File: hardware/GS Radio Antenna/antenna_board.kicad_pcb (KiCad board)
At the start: 2 copper layers, 100 x 100 mm, 22 parts, among them J1 Conn_01x02_Socket, U10 IRF4905PBF, U11 IRF4905PBF, U12 IRF4905PBF, U2 ESP32-DEVKITC, U3 LM3940IT-3.3/NOPB, U4 TLC5916IN, U5 TLC5916IN, U6 TLC5916IN, U9 IRF4905PBF

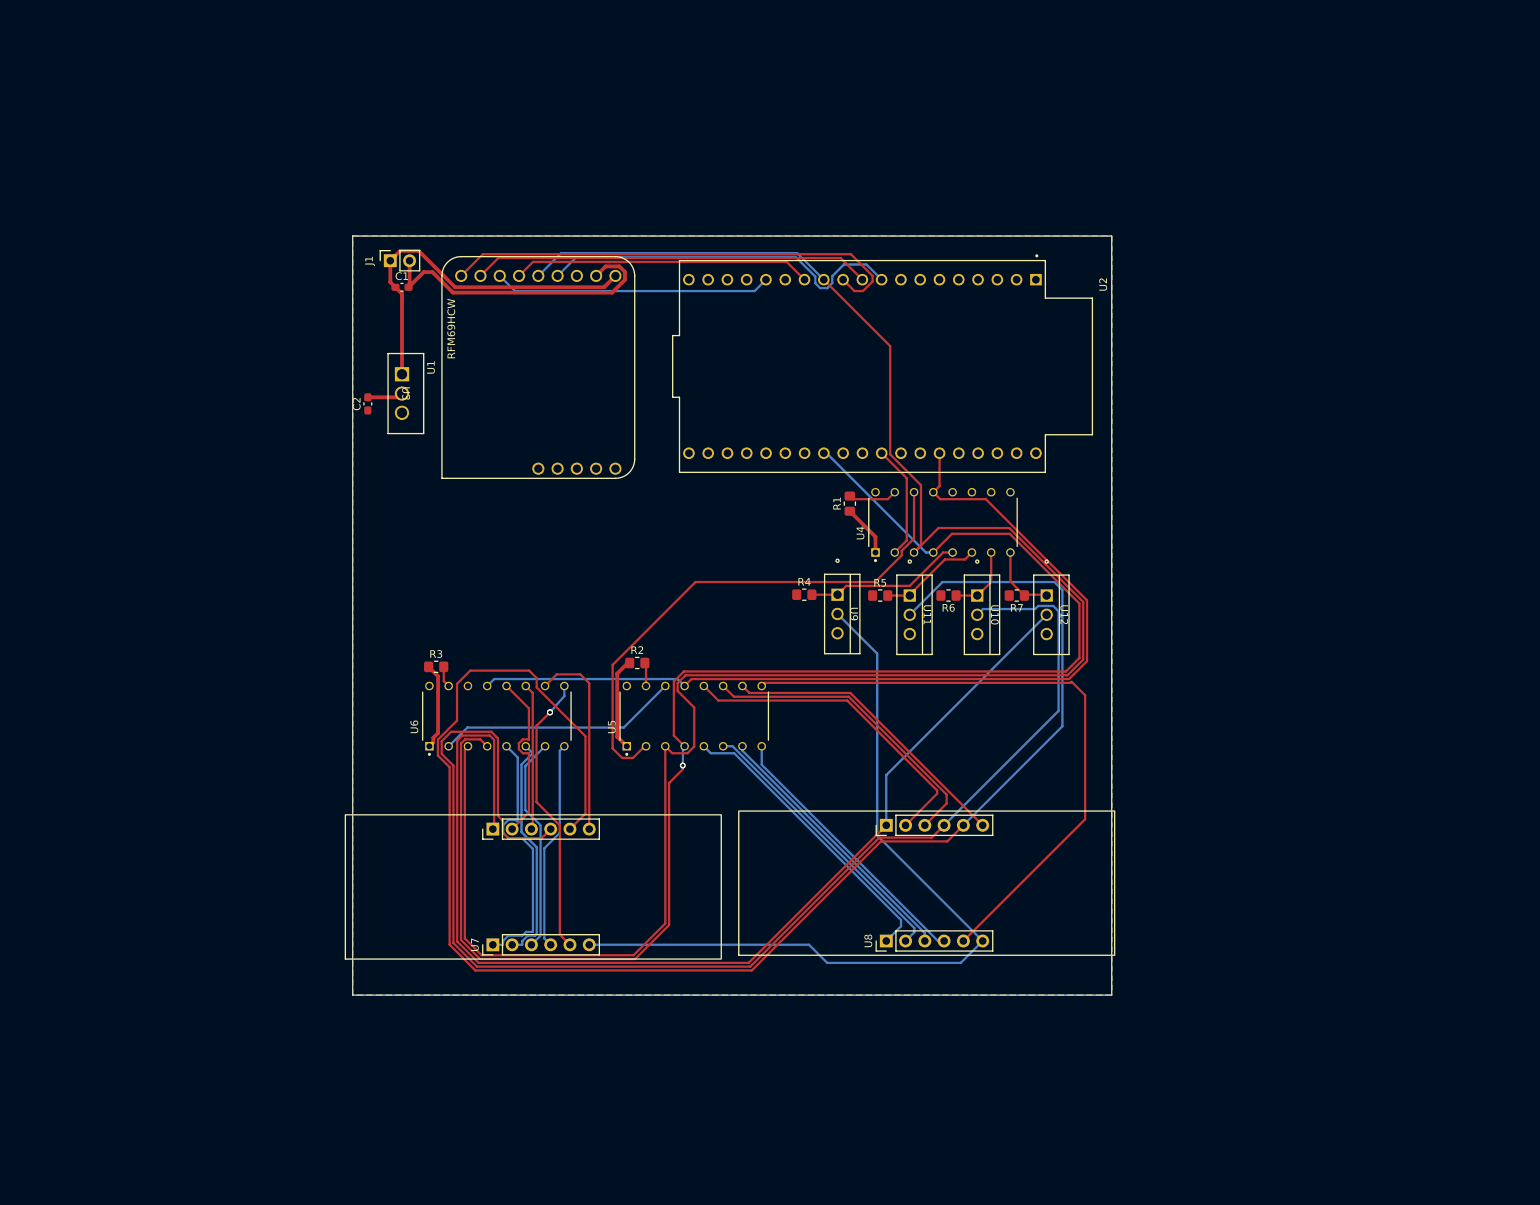
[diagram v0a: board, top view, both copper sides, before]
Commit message: New GS Radio board layout without wiring
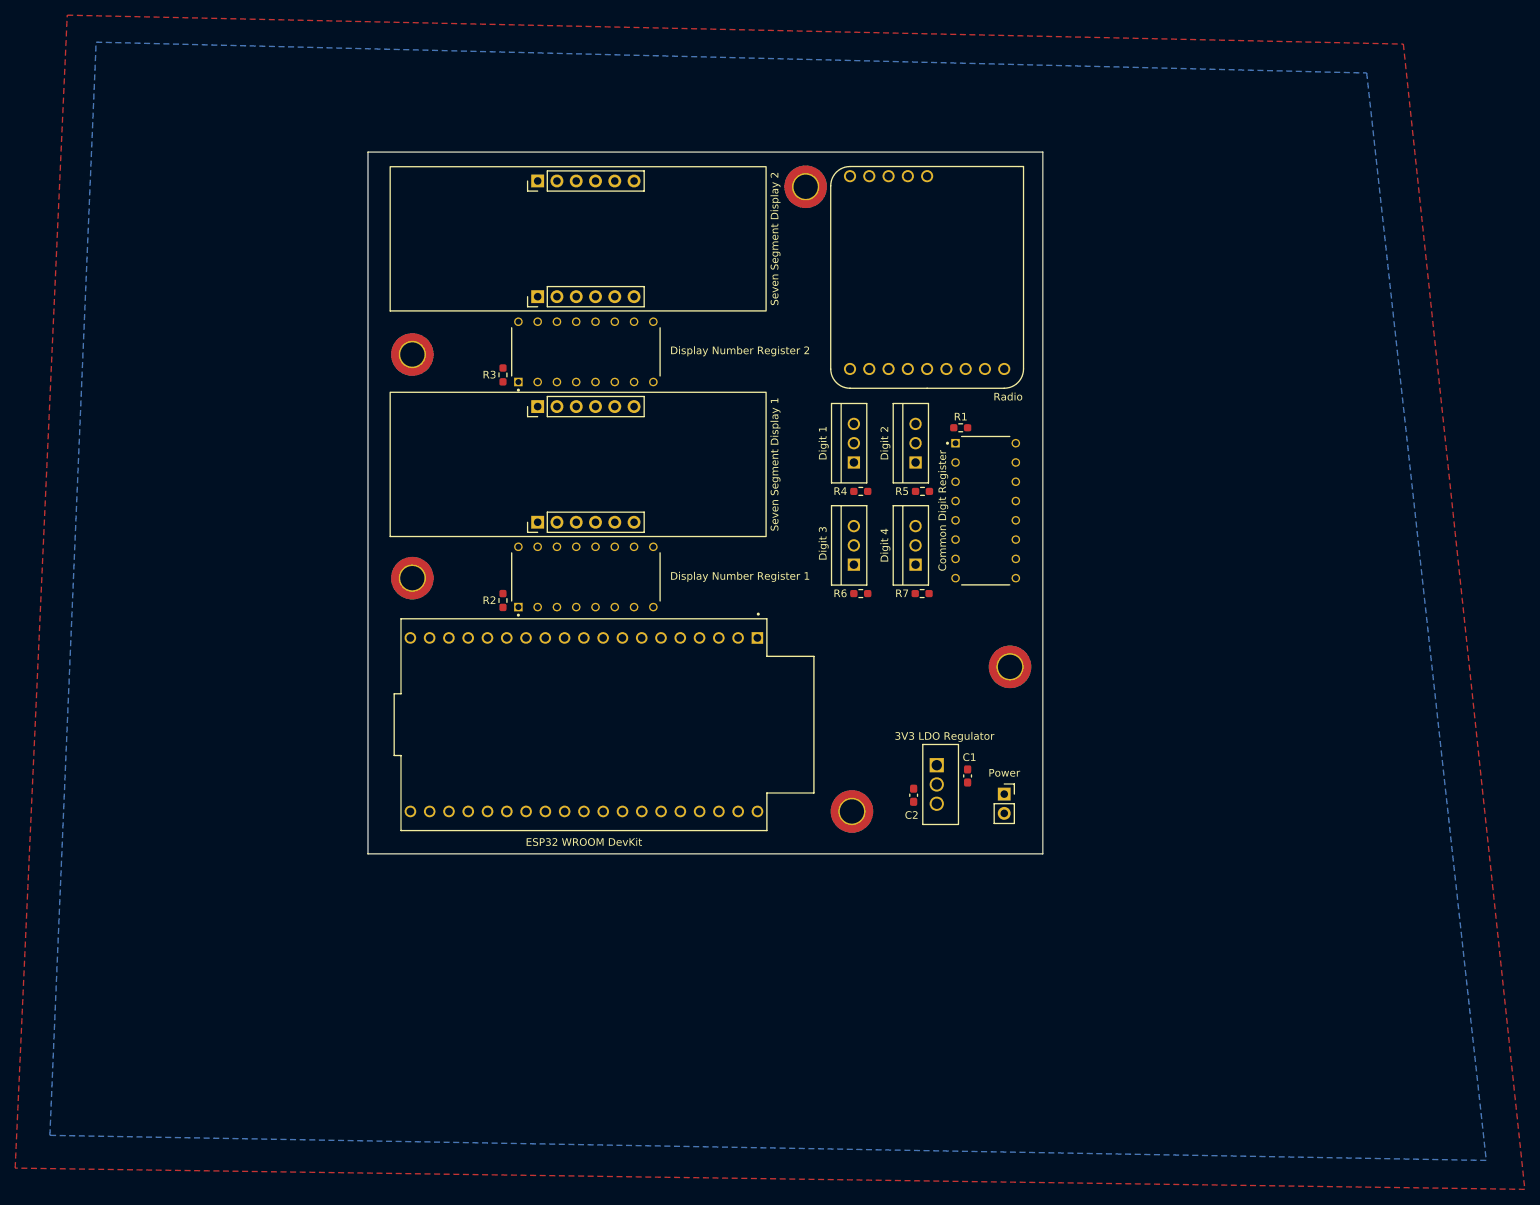
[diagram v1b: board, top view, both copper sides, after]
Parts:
- removed J1: Conn_01x02_Socket, Connector_PinSocket_2.54mm:PinSocket_1x02_P2.54mm_Vertical
- removed U1: ~, Rocketry:RFM69HCW_Breakout
- removed U10, U11, U12, U9: IRF4905PBF, rocketry_footprints:PG-TO220-3_INF
- removed U2: ESP32-DEVKITC, ESP32_devkit_C:MODULE_ESP32-DEVKITC
- removed U3: LM3940IT-3.3/NOPB, Rocketry:T03B
- removed U4, U5, U6: TLC5916IN, TLC5916IN:DIP794W45P254L1969H508Q16
- removed U7, U8: ~, Rocketry:PinHeader_1x06_P2.54mm_Vertical
- added 3V3 LDO Regulator: LM3940IT-3.3/NOPB, rocketry_footprints:LM3940IT, F.Cu at (176.3, 127.8)
- added Common Digit Register: TLC5916IN, rocketry_footprints:TLC5916IN, F.Cu at (181.7, 89.2)
- added Digit 1: IRF4905PBF, rocketry_footprints:PG-TO220-3_INF, F.Cu at (164.3, 82.8)
- added Digit 2: IRF4905PBF, rocketry_footprints:PG-TO220-3_INF, F.Cu at (172.5, 82.8)
- added Digit 3: IRF4905PBF, rocketry_footprints:PG-TO220-3_INF, F.Cu at (164.3, 96.3)
- added Digit 4: IRF4905PBF, rocketry_footprints:PG-TO220-3_INF, F.Cu at (172.5, 96.3)
- added Display Number Register 1: TLC5916IN, rocketry_footprints:TLC5916IN, F.Cu at (129.0, 97.9)
- added Display Number Register 2: TLC5916IN, rocketry_footprints:TLC5916IN, F.Cu at (129.0, 68.2)
- added ESP32 WROOM DevKit: ESP32-DEVKITC, rocketry_footprints:MODULE_ESP32-DEVKITC, F.Cu at (128.8, 117.3)
- added H1: MountingHole, MountingHole:MountingHole_3.2mm_M3_DIN965_Pad_TopBottom, F.Cu at (106.2, 68.6)
- added H2: MountingHole, MountingHole:MountingHole_3.2mm_M3_DIN965_Pad_TopBottom, F.Cu at (106.2, 98.0)
- added H3: MountingHole, MountingHole:MountingHole_3.2mm_M3_DIN965_Pad_TopBottom, F.Cu at (158.0, 46.5)
- added H4: MountingHole, MountingHole:MountingHole_3.2mm_M3_DIN965_Pad_TopBottom, F.Cu at (184.9, 109.7)
- added H5: MountingHole, MountingHole:MountingHole_3.2mm_M3_DIN965_Pad_TopBottom, F.Cu at (164.1, 128.8)
- added Power: Conn_01x02_Socket, Connector_PinSocket_2.54mm:PinSocket_1x02_P2.54mm_Vertical, F.Cu at (184.2, 126.5)
- added Radio: ~, rocketry_footprints:RFM69HCW_Breakout, F.Cu at (174.0, 58.4)
- added Seven Segment Display 1: ~, rocketry_footprints:Seven_Segment_Display, F.Cu at (122.7, 90.7)
- added Seven Segment Display 2: ~, rocketry_footprints:Seven_Segment_Display, F.Cu at (122.7, 61.0)
- R1, R2, R3, R4, R5, R6, R7: footprint Resistor_SMD:R_0805_2012Metric_Pad1.20x1.40mm_HandSolder -> Resistor_SMD:R_0603_1608Metric_Pad0.98x0.95mm_HandSolder
- moved C1 98.5 mm to (179.3, 124.1), turned to -90 degrees
- moved C2 88.5 mm to (172.2, 126.6)
- moved R3 39.4 mm to (118.1, 71.3), turned to 90 degrees
- moved R2 19.5 mm to (118.1, 101.0), turned to 90 degrees
- moved R1 17.7 mm to (178.4, 78.2), turned to 0 degrees
- moved R4 15.5 mm to (165.3, 86.6), turned to 180 degrees
- moved R5 14.8 mm to (173.4, 86.6), turned to 180 degrees
- moved R7 12.5 mm to (173.3, 100.1), turned to 0 degrees
- moved R6 11.6 mm to (165.3, 100.1), turned to 0 degrees
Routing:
- net /SCK: track 263.6 -> 0.00 mm
- net /CTL2: track 207.7 -> 0.00 mm
- net /LE: track 199.6 -> 0.00 mm, vias 1 -> 0
- net /CTL3: track 174.9 -> 0.00 mm
- net /CTL4: track 145.3 -> 0.00 mm
- net /OE: track 120.8 -> 0.00 mm
- net /CTL1: track 105.0 -> 0.00 mm
- net /71_5: track 82.6 -> 0.00 mm
- net GND: track 75.7 -> 0.00 mm
- net Net-(U4-SDO): track 69.6 -> 0.00 mm
- net /RST: track 62.3 -> 0.00 mm
- net /CS: track 52.5 -> 0.00 mm
- net /G0: track 48.6 -> 0.00 mm
- net VDD: track 48.4 -> 0.00 mm
- net /71_8: track 42.7 -> 0.00 mm
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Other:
- board size 100 x 100 mm -> 88.9 x 92.5 mm

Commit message: Finished GS Radio layout
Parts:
- U10: renamed from Digit 3
- U11: renamed from Digit 2
- U12: renamed from Digit 4
- U2: renamed from ESP32 WROOM DevKit
- U3: renamed from 3V3 LDO Regulator
- U4: renamed from Common Digit Register
- U5: renamed from Display Number Register 1
- U6: renamed from Display Number Register 2
- U7: renamed from Seven Segment Display 2
- U8: renamed from Seven Segment Display 1
- U9: renamed from Digit 1
- moved U10 15.7 mm to (172.5, 82.8)
- moved U11 15.7 mm to (164.3, 96.3)
- moved R5 15.7 mm to (165.3, 100.1)
- moved R6 15.7 mm to (173.4, 86.6)
- renumbered Power to J1, Radio to U1
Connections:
- U2 pad 14: unconnected-(U2-GND1-Pad14) -> GND
- U2 pad 31: unconnected-(U2-IO19-Pad31) -> /CLK
- U2 pad 32: unconnected-(U2-GND2-Pad32) -> GND
- U2 pad 38: unconnected-(U2-GND3-Pad38) -> GND
- U4 pad 3: /SCK -> /CLK
- U5 pad 3: /SCK -> /CLK
- U6 pad 3: /SCK -> /CLK
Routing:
- net /3.3V: track 0.00 -> 268.7 mm, vias 0 -> 5
- net GND: track 0.00 -> 262.9 mm
- net /OE: track 0.00 -> 187.5 mm, vias 0 -> 9
- net /CLK: track 0.00 -> 141.9 mm, vias 0 -> 9
- net /CTL4: track 0.00 -> 123.4 mm, vias 0 -> 3
- net /LE: track 0.00 -> 113.5 mm, vias 0 -> 11
- net /G0: track 0.00 -> 103.4 mm, vias 0 -> 4
- net /MOSI: track 0.00 -> 102.0 mm, vias 0 -> 1
- net /RST: track 0.00 -> 98.9 mm, vias 0 -> 2
- net /CS: track 0.00 -> 96.8 mm, vias 0 -> 2
- net /MISO: track 0.00 -> 96.7 mm, vias 0 -> 1
- net /CTL3: track 0.00 -> 96.1 mm
- net /SCK: track 0.00 -> 95.0 mm
- net /CTL2: track 0.00 -> 94.8 mm, vias 0 -> 2
- net Net-(U4-SDO): track 0.00 -> 93.7 mm, vias 0 -> 3
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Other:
- board text added: "3V3 LDO Regulator"
- board text added: "Common Digit Register"
- board text added: "Digit 1"
- board text added: "Digit 2"
- board text added: "Digit 3"
- board text added: "Digit 4"
- board text added: "Display Number Register 1"
- board text added: "Display Number Register 2"
- board text added: "ESP32 WROOM DevKit"
- board text added: "Power"
- board text added: "Radio"
- board text added: "Seven Segment Display 1"
- board text added: "Seven Segment Display 2"

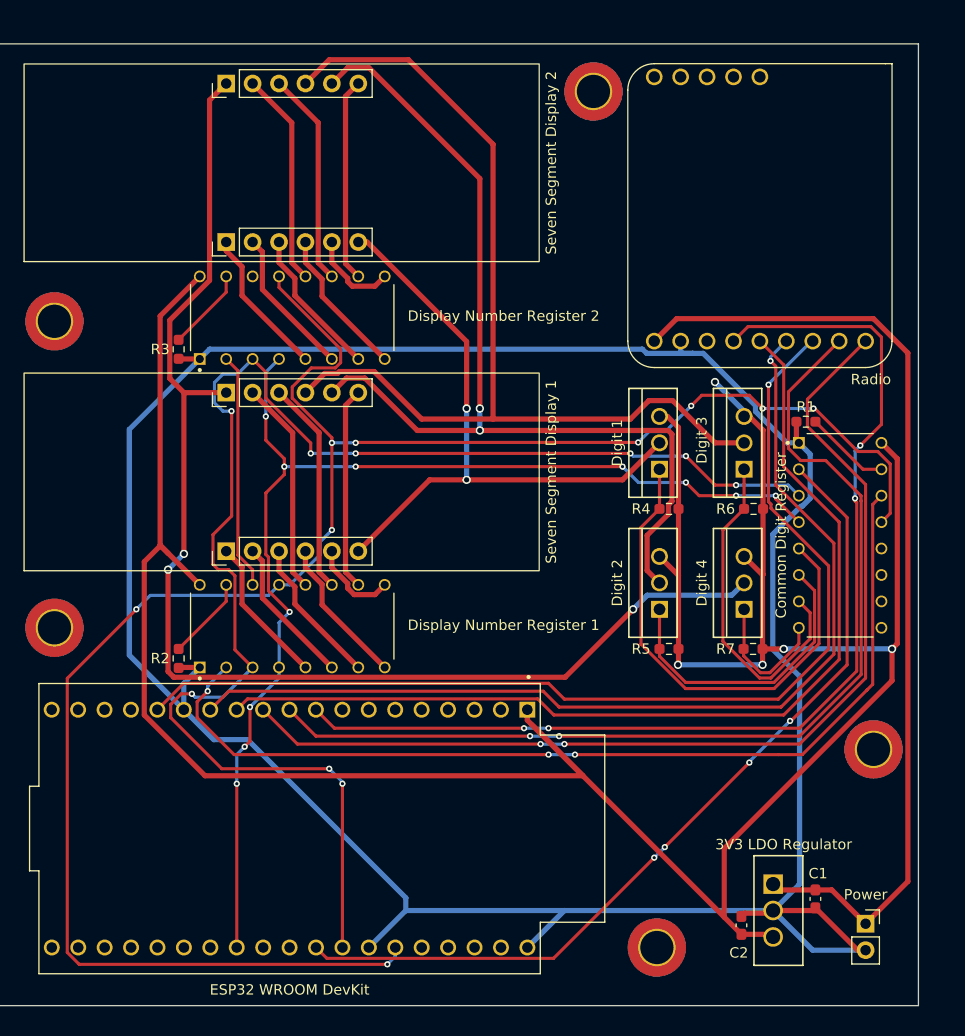
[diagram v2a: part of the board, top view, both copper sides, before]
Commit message: Adjusted GS Radio track and via spacing
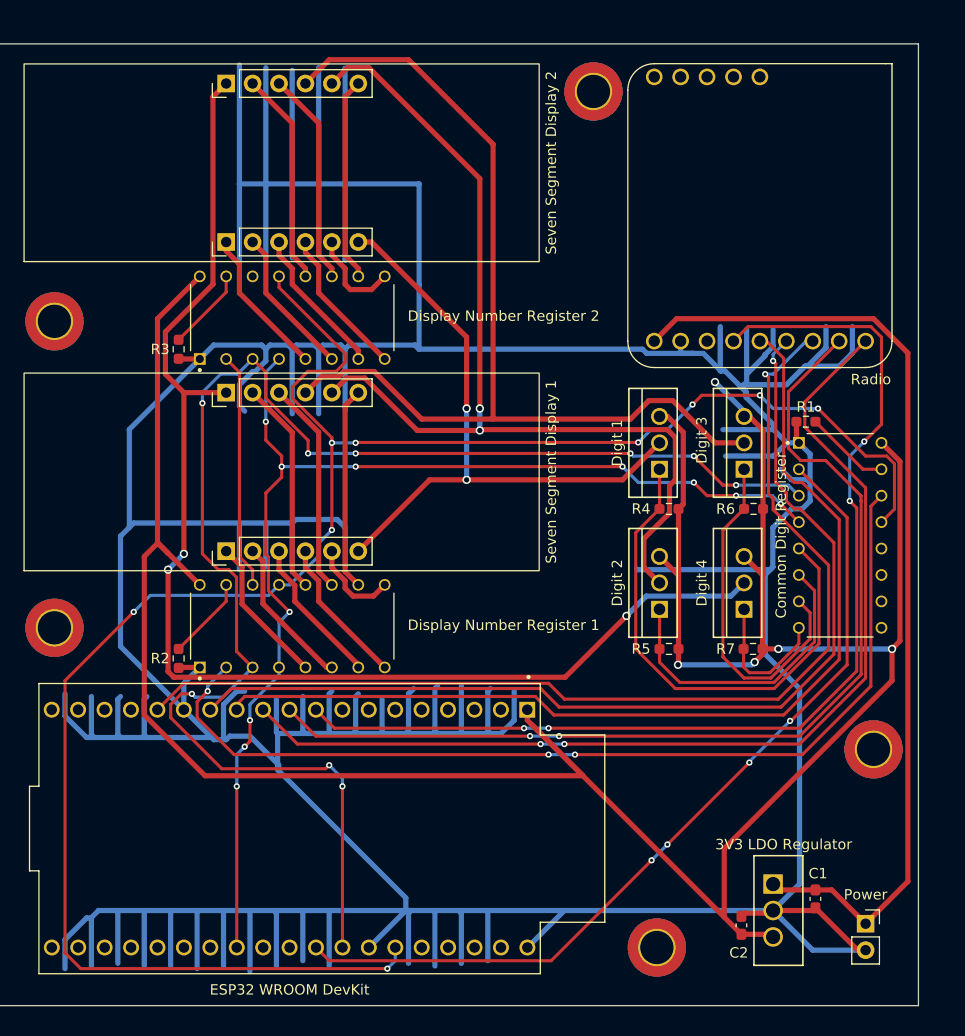
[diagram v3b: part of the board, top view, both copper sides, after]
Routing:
- net GND: track 262.9 -> 730.8 mm
- net /OE: track 187.5 -> 189.6 mm
- net /SCK: track 95.0 -> 96.3 mm
- net /MOSI: track 102.0 -> 103.0 mm
- net /MOS1: track 48.2 -> 49.2 mm
- net /MOS3: track 32.8 -> 33.7 mm
- net /3.3V: track 268.7 -> 269.5 mm
- net /MOS4: track 13.2 -> 13.8 mm
- net /CTL2: track 94.8 -> 95.4 mm
- net /72_5: track 8.57 -> 9.14 mm

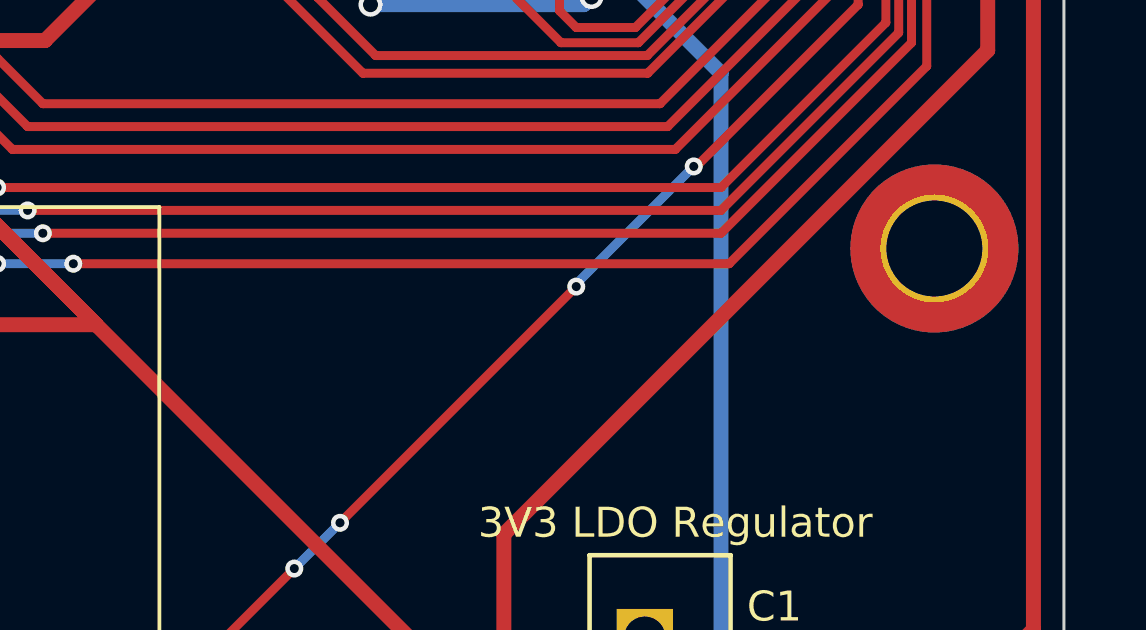
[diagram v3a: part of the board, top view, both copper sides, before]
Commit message: Add credits and aesthetics to GS Radio
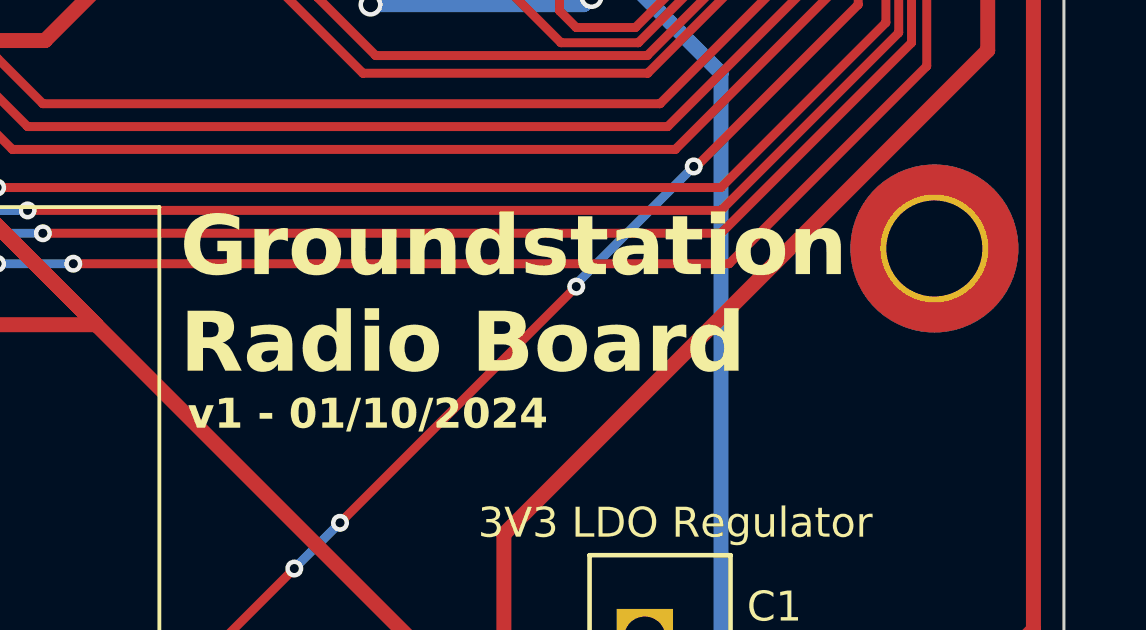
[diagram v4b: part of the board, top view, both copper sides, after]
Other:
- board text added: "Alex Mineeva"
- board text added: "Ari Bobesh"
- board text added: "DESIGN BY"
- board text added: "Daniel Theunissen"
- board text added: "Ertug Umsur"
- board text added: "Groundstation Radio Board"
- board text added: "Ishan Porwal"
- board text added: "Joseph Liu"
- board text added: "Mateo Brancoli"
- board text added: "Nividh Singh"
- board text added: "Rohan Shah"
- board text added: "Rowan Jansens"
- board text added: "v1 - 01/10/2024"
